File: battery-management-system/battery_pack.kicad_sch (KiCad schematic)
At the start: 26 parts, among them J1 CELL4_PLUS, J10 VBAT+_CHARGE, J2 CELL4_MINUS, J3 CELL3_MINUS, J4 CELL2_MINUS, J5 CELL1_MINUS, J6 VBAT+, J8 VBAT-, Q1 DMN3730U, Q10 DMN3730U, Q2 TJ40S04M3L, Q3 TJ40S04M3L, Q4 DMN3730U

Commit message: improve layout
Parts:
- renumbered D8 to D3, D9 to D4, D13 to D5, D14 to D6, J10 to J7, Q10 to Q5, R46 to R4, R47 to R5
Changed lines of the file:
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@@
   (symbol (lib_id "benediktibk:SBR2065D1") (at 172.72 44.45 0) (mirror y) (unit 1)
     (in_bom yes) (on_board yes) (dnp no) (fields_autoplaced)
-    (property "Reference" "D8" (at 173.0375 38.1 0)
+    (property "Reference" "D3" (at 173.0375 38.1 0)
       (effects (font (size 1.27 1.27)))
     )
@@
       (project "battery-management-system"
         (path "/5272f0ff-3069-41a9-bca2-80beede8b4b2/31b87c35-c096-4dc0-8978-834bec283b57"
-          (reference "D8") (unit 1)
+          (reference "D3") (unit 1)
         )
       )
@@
   (symbol (lib_id "benediktibk:SBR2065D1") (at 226.06 69.85 90) (mirror x) (unit 1)
     (in_bom yes) (on_board yes) (dnp no) (fields_autoplaced)
-    (property "Reference" "D14" (at 228.6 68.2625 90)
+    (property "Reference" "D6" (at 228.6 68.2625 90)
       (effects (font (size 1.27 1.27)) (justify right))
     )
@@
       (project "battery-management-system"
         (path "/5272f0ff-3069-41a9-bca2-80beede8b4b2/31b87c35-c096-4dc0-8978-834bec283b57"
-          (reference "D14") (unit 1)
+          (reference "D6") (unit 1)
         )
       )
@@
   (symbol (lib_id "benediktibk:SBR2065D1") (at 172.72 53.34 0) (unit 1)
     (in_bom yes) (on_board yes) (dnp no) (fields_autoplaced)
-    (property "Reference" "D9" (at 172.4025 46.99 0)
+    (property "Reference" "D4" (at 172.4025 46.99 0)
       (effects (font (size 1.27 1.27)))
     )
@@
       (project "battery-management-system"
         (path "/5272f0ff-3069-41a9-bca2-80beede8b4b2/31b87c35-c096-4dc0-8978-834bec283b57"
-          (reference "D9") (unit 1)
+          (reference "D4") (unit 1)
         )
       )
@@
   (symbol (lib_id "benediktibk:SBR2065D1") (at 218.44 60.96 90) (mirror x) (unit 1)
     (in_bom yes) (on_board yes) (dnp no) (fields_autoplaced)
-    (property "Reference" "D13" (at 220.98 59.3725 90)
+    (property "Reference" "D5" (at 220.98 59.3725 90)
       (effects (font (size 1.27 1.27)) (justify right))
     )
@@
       (project "battery-management-system"
         (path "/5272f0ff-3069-41a9-bca2-80beede8b4b2/31b87c35-c096-4dc0-8978-834bec283b57"
-          (reference "D13") (unit 1)
+          (reference "D5") (unit 1)
         )
       )
@@
   (symbol (lib_id "power:GND") (at 144.78 97.79 0) (unit 1)
     (in_bom yes) (on_board yes) (dnp no) (fields_autoplaced)
-    (property "Reference" "#PWR0101" (at 144.78 104.14 0)
+    (property "Reference" "#PWR06" (at 144.78 104.14 0)
       (effects (font (size 1.27 1.27)) hide)
     )
@@
       (project "battery-management-system"
         (path "/5272f0ff-3069-41a9-bca2-80beede8b4b2/31b87c35-c096-4dc0-8978-834bec283b57"
-          (reference "#PWR0101") (unit 1)
+          (reference "#PWR06") (unit 1)
         )
       )
@@
   (symbol (lib_id "benediktibk:R_10kOhm_SMD_0603_100mW_1%") (at 196.85 69.85 0) (unit 1)
     (in_bom yes) (on_board yes) (dnp no) (fields_autoplaced)
-    (property "Reference" "R47" (at 199.39 68.58 0)
+    (property "Reference" "R5" (at 199.39 68.58 0)
       (effects (font (size 1.27 1.27)) (justify left))
     )
@@
       (project "battery-management-system"
         (path "/5272f0ff-3069-41a9-bca2-80beede8b4b2/31b87c35-c096-4dc0-8978-834bec283b57"
-          (reference "R47") (unit 1)
+          (reference "R5") (unit 1)
         )
       )
@@
   (symbol (lib_id "power:GND") (at 95.25 97.79 0) (unit 1)
     (in_bom yes) (on_board yes) (dnp no) (fields_autoplaced)
-    (property "Reference" "#PWR0102" (at 95.25 104.14 0)
+    (property "Reference" "#PWR05" (at 95.25 104.14 0)
       (effects (font (size 1.27 1.27)) hide)
     )
@@
       (project "battery-management-system"
         (path "/5272f0ff-3069-41a9-bca2-80beede8b4b2/31b87c35-c096-4dc0-8978-834bec283b57"
-          (reference "#PWR0102") (unit 1)
+          (reference "#PWR05") (unit 1)
         )
       )
@@
   (symbol (lib_id "benediktibk:DMN3730U") (at 194.31 82.55 0) (unit 1)
     (in_bom yes) (on_board yes) (dnp no) (fields_autoplaced)
-    (property "Reference" "Q10" (at 200.66 81.2799 0)
+    (property "Reference" "Q5" (at 200.66 81.2799 0)
       (effects (font (size 1.27 1.27)) (justify left))
     )
@@
       (project "battery-management-system"
         (path "/5272f0ff-3069-41a9-bca2-80beede8b4b2/31b87c35-c096-4dc0-8978-834bec283b57"
-          (reference "Q10") (unit 1)
+          (reference "Q5") (unit 1)
         )
       )
@@
   (symbol (lib_id "power:GND") (at 40.64 143.51 0) (unit 1)
     (in_bom yes) (on_board yes) (dnp no) (fields_autoplaced)
-    (property "Reference" "#PWR0103" (at 40.64 149.86 0)
+    (property "Reference" "#PWR04" (at 40.64 149.86 0)
       (effects (font (size 1.27 1.27)) hide)
     )
@@
       (project "battery-management-system"
         (path "/5272f0ff-3069-41a9-bca2-80beede8b4b2/31b87c35-c096-4dc0-8978-834bec283b57"
-          (reference "#PWR0103") (unit 1)
+          (reference "#PWR04") (unit 1)
         )
       )
@@
     )
   )
-  (symbol (lib_name "TJ40S04M3L_1") (lib_id "benediktibk:TJ40S04M3L") (at 135.89 46.99 270) (mirror x) (unit 1)
+  (symbol (lib_id "benediktibk:TJ40S04M3L") (at 135.89 46.99 270) (mirror x) (unit 1)
     (in_bom yes) (on_board yes) (dnp no) (fields_autoplaced)
     (property "Reference" "Q3" (at 135.89 36.83 90)
@@
     )
   )
-  (symbol (lib_name "R_220kOhm_SMD_0603_100mW_1%_1") (lib_id "benediktibk:R_220kOhm_SMD_0603_100mW_1%") (at 144.78 66.04 0) (unit 1)
+  (symbol (lib_id "benediktibk:R_220kOhm_SMD_0603_100mW_1%") (at 144.78 66.04 0) (unit 1)
     (in_bom yes) (on_board yes) (dnp no)
     (property "Reference" "R3" (at 147.32 64.7699 0)
@@
   (symbol (lib_id "power:GND") (at 184.15 99.06 0) (unit 1)
     (in_bom yes) (on_board yes) (dnp no) (fields_autoplaced)
-    (property "Reference" "#PWR015" (at 184.15 105.41 0)
+    (property "Reference" "#PWR07" (at 184.15 105.41 0)
       (effects (font (size 1.27 1.27)) hide)
     )
@@
       (project "battery-management-system"
         (path "/5272f0ff-3069-41a9-bca2-80beede8b4b2/31b87c35-c096-4dc0-8978-834bec283b57"
-          (reference "#PWR015") (unit 1)
+          (reference "#PWR07") (unit 1)
         )
       )
@@
     )
   )
-  (symbol (lib_name "BAT54WS_1") (lib_id "benediktibk:BAT54WS") (at 144.78 52.07 90) (unit 1)
+  (symbol (lib_id "benediktibk:BAT54WS") (at 144.78 52.07 90) (unit 1)
     (in_bom yes) (on_board yes) (dnp no) (fields_autoplaced)
     (property "Reference" "D2" (at 147.32 51.1174 90)
@@
   (symbol (lib_id "power:GND") (at 196.85 99.06 0) (unit 1)
     (in_bom yes) (on_board yes) (dnp no) (fields_autoplaced)
-    (property "Reference" "#PWR014" (at 196.85 105.41 0)
+    (property "Reference" "#PWR08" (at 196.85 105.41 0)
       (effects (font (size 1.27 1.27)) hide)
     )
@@
       (project "battery-management-system"
         (path "/5272f0ff-3069-41a9-bca2-80beede8b4b2/31b87c35-c096-4dc0-8978-834bec283b57"
-          (reference "#PWR014") (unit 1)
+          (reference "#PWR08") (unit 1)
         )
       )
@@
   (symbol (lib_id "benediktibk:Connector_M6") (at 267.97 53.34 0) (unit 1)
     (in_bom yes) (on_board yes) (dnp no) (fields_autoplaced)
-    (property "Reference" "J10" (at 270.51 52.0699 0)
+    (property "Reference" "J7" (at 270.51 52.0699 0)
       (effects (font (size 1.27 1.27)) (justify left))
     )
@@
       (project "battery-management-system"
         (path "/5272f0ff-3069-41a9-bca2-80beede8b4b2/31b87c35-c096-4dc0-8978-834bec283b57"
-          (reference "J10") (unit 1)
+          (reference "J7") (unit 1)
         )
       )
@@
   (symbol (lib_id "power:GND") (at 226.06 93.98 0) (unit 1)
     (in_bom yes) (on_board yes) (dnp no) (fields_autoplaced)
-    (property "Reference" "#PWR0116" (at 226.06 100.33 0)
+    (property "Reference" "#PWR09" (at 226.06 100.33 0)
       (effects (font (size 1.27 1.27)) hide)
     )
@@
       (project "battery-management-system"
         (path "/5272f0ff-3069-41a9-bca2-80beede8b4b2/31b87c35-c096-4dc0-8978-834bec283b57"
-          (reference "#PWR0116") (unit 1)
+          (reference "#PWR09") (unit 1)
         )
       )
@@
   (symbol (lib_id "benediktibk:R_10kOhm_SMD_0603_100mW_1%") (at 184.15 90.17 0) (unit 1)
     (in_bom yes) (on_board yes) (dnp no) (fields_autoplaced)
-    (property "Reference" "R46" (at 186.69 88.9 0)
+    (property "Reference" "R4" (at 186.69 88.9 0)
       (effects (font (size 1.27 1.27)) (justify left))
     )
@@
       (project "battery-management-system"
         (path "/5272f0ff-3069-41a9-bca2-80beede8b4b2/31b87c35-c096-4dc0-8978-834bec283b57"
-          (reference "R46") (unit 1)
-        )
-      )
+          (reference "R4") (unit 1)
+        )
+      )

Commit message: improve silkscreen and fab
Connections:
- net CELL1_MINUS: now also R1.1
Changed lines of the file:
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@@
   (junction (at 184.15 53.34) (diameter 0) (color 0 0 0 0)
+  )
+  (junction (at 40.64 113.03) (diameter 0) (color 0 0 0 0)
   )
   (junction (at 226.06 86.36) (diameter 0) (color 0 0 0 0)
@@
     (stroke (width 0) (type default))
   )
-  (wire (pts (xy 36.83 113.03) (xy 52.07 113.03))
+  (wire (pts (xy 36.83 113.03) (xy 40.64 113.03))
     (stroke (width 0) (type default))
   )
@@
     (stroke (width 0) (type default))
   )
-  (wire (pts (xy 40.64 113.03) (xy 40.64 124.46))
-    (stroke (width 0) (type default))
-  )
   (wire (pts (xy 158.75 44.45) (xy 168.91 44.45))
     (stroke (width 0) (type default))
@@
     (stroke (width 0) (type default))
   )
+  (wire (pts (xy 40.64 113.03) (xy 52.07 113.03))
+    (stroke (width 0) (type default))
+  )
   (wire (pts (xy 196.85 76.2) (xy 198.12 76.2))
     (stroke (width 0) (type default))
@@
     (stroke (width 0) (type default))
   )
+  (wire (pts (xy 40.64 113.03) (xy 40.64 124.46))
+    (stroke (width 0) (type default))
+  )

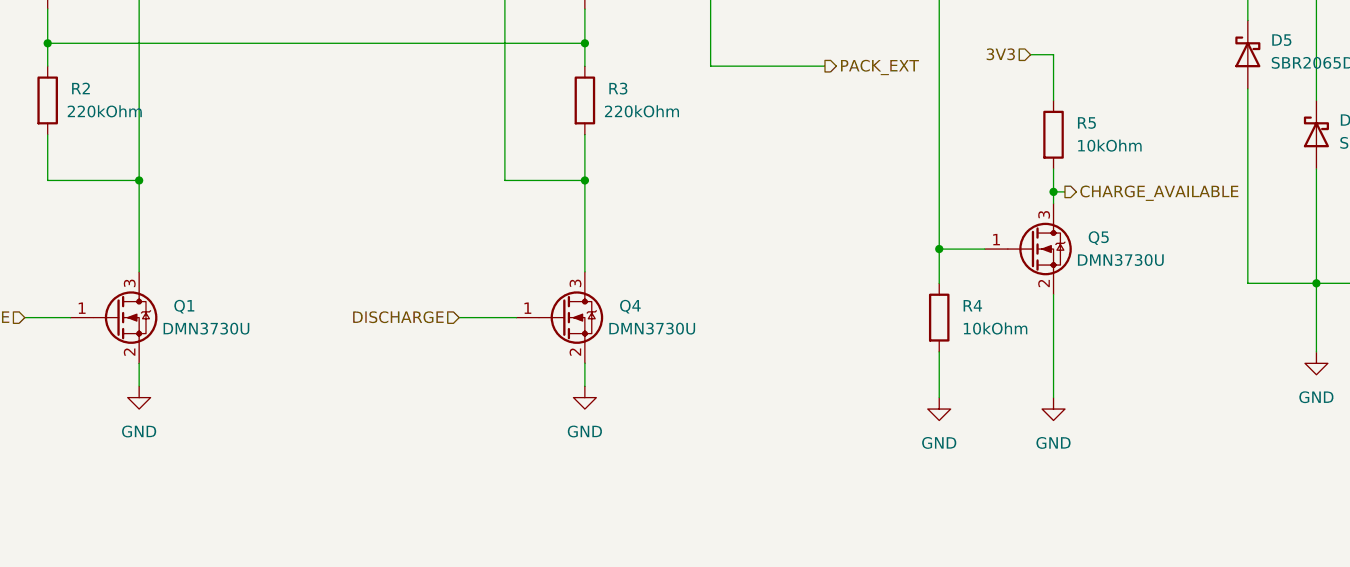
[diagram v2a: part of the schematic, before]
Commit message: switch to inductor based cell balancing
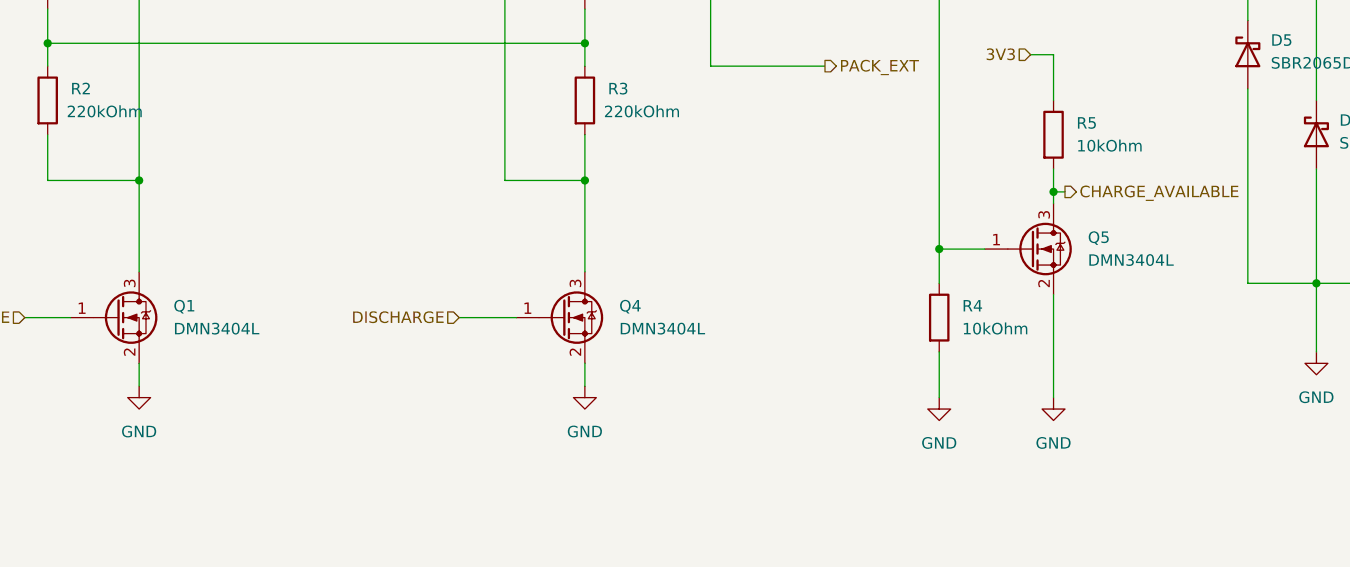
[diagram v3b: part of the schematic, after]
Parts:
- Q1, Q4, Q5: value DMN3730U -> DMN3404L; symbol benediktibk:DMN3730U -> benediktibk:DMN3404L; RS order number 823-2946 -> 751-4171
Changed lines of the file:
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@@
     )
   )
-  (symbol (lib_id "benediktibk:DMN3730U") (at 194.31 82.55 0) (unit 1)
-    (in_bom yes) (on_board yes) (dnp no) (fields_autoplaced)
-    (property "Reference" "Q5" (at 200.66 81.2799 0)
-      (effects (font (size 1.27 1.27)) (justify left))
-    )
-    (property "Value" "DMN3730U" (at 199.39 83.82 0)
+  (symbol (lib_id "benediktibk:DMN3404L") (at 194.31 82.55 0) (unit 1)
+    (in_bom yes) (on_board yes) (dnp no) (fields_autoplaced)
+    (property "Reference" "Q5" (at 200.66 81.28 0)
+      (effects (font (size 1.27 1.27)) (justify left))
+    )
+    (property "Value" "DMN3404L" (at 200.66 83.82 0)
       (effects (font (size 1.27 1.27)) (justify left))
     )
@@
       (effects (font (size 1.27 1.27)) hide)
     )
-    (property "RS order number" "823-2946" (at 194.31 82.55 0)
+    (property "RS order number" "751-4171" (at 191.77 87.63 0)
       (effects (font (size 1.27 1.27)) hide)
     )
@@
     )
   )
-  (symbol (lib_id "benediktibk:DMN3730U") (at 142.24 90.17 0) (unit 1)
-    (in_bom yes) (on_board yes) (dnp no) (fields_autoplaced)
-    (property "Reference" "Q4" (at 148.59 88.8999 0)
-      (effects (font (size 1.27 1.27)) (justify left))
-    )
-    (property "Value" "DMN3730U" (at 147.32 91.44 0)
+  (symbol (lib_id "benediktibk:DMN3404L") (at 142.24 90.17 0) (unit 1)
+    (in_bom yes) (on_board yes) (dnp no) (fields_autoplaced)
+    (property "Reference" "Q4" (at 148.59 88.9 0)
+      (effects (font (size 1.27 1.27)) (justify left))
+    )
+    (property "Value" "DMN3404L" (at 148.59 91.44 0)
       (effects (font (size 1.27 1.27)) (justify left))
     )
@@
       (effects (font (size 1.27 1.27)) hide)
     )
-    (property "RS order number" "823-2946" (at 142.24 90.17 0)
+    (property "RS order number" "751-4171" (at 139.7 95.25 0)
       (effects (font (size 1.27 1.27)) hide)
     )
@@
     )
   )
-  (symbol (lib_id "benediktibk:DMN3730U") (at 92.71 90.17 0) (unit 1)
-    (in_bom yes) (on_board yes) (dnp no) (fields_autoplaced)
-    (property "Reference" "Q1" (at 99.06 88.8999 0)
-      (effects (font (size 1.27 1.27)) (justify left))
-    )
-    (property "Value" "DMN3730U" (at 97.79 91.44 0)
+  (symbol (lib_id "benediktibk:DMN3404L") (at 92.71 90.17 0) (unit 1)
+    (in_bom yes) (on_board yes) (dnp no) (fields_autoplaced)
+    (property "Reference" "Q1" (at 99.06 88.9 0)
+      (effects (font (size 1.27 1.27)) (justify left))
+    )
+    (property "Value" "DMN3404L" (at 99.06 91.44 0)
       (effects (font (size 1.27 1.27)) (justify left))
     )
@@
       (effects (font (size 1.27 1.27)) hide)
     )
-    (property "RS order number" "823-2946" (at 92.71 90.17 0)
-      (effects (font (size 1.27 1.27)) hide)
-    )
+    (property "RS order number" "751-4171" (at 90.17 95.25 0)
+      (effects (font (size 1.27 1.27)) hide)
+    )
